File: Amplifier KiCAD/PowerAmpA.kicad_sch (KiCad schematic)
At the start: 39 parts, among them Q1 BC546, Q10 TIP36, Q2 BC546, Q3 BCM846BS-7, Q4 BC546, Q5 BD140, Q6 BC546, Q7 BD140, Q8 TIP35, Q9 BD139

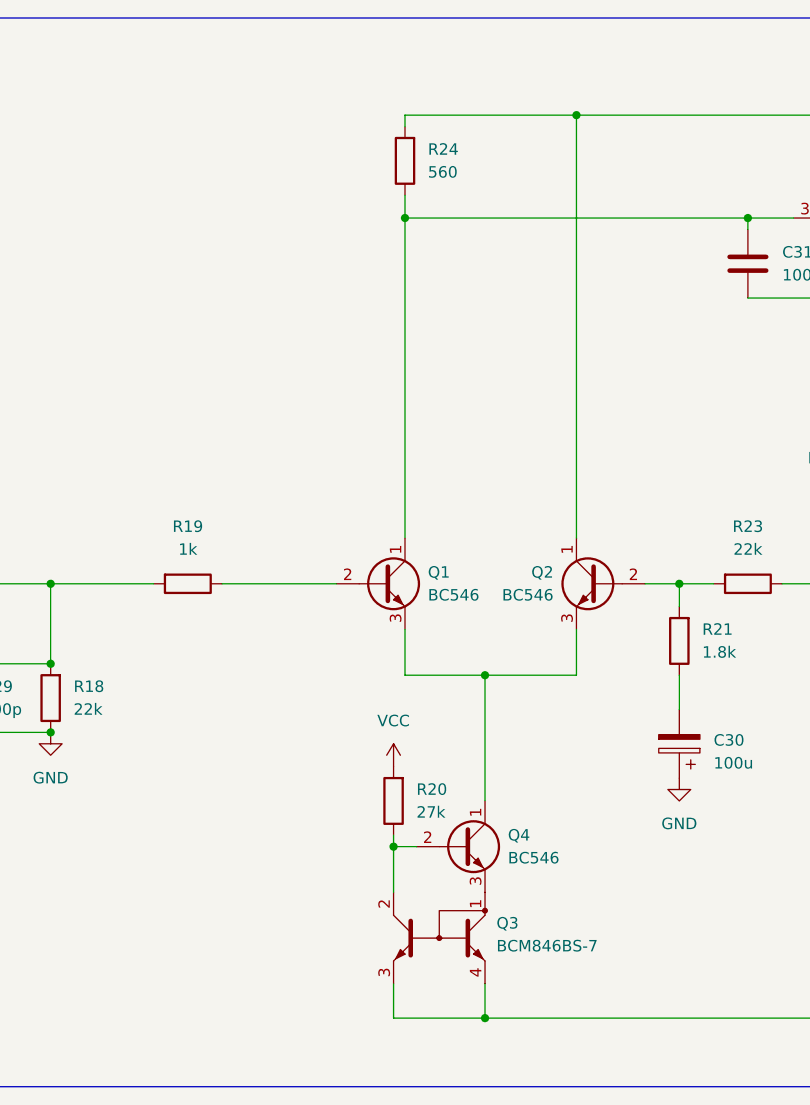
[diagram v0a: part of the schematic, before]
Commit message: Component Placement Finalised, Starting Traces
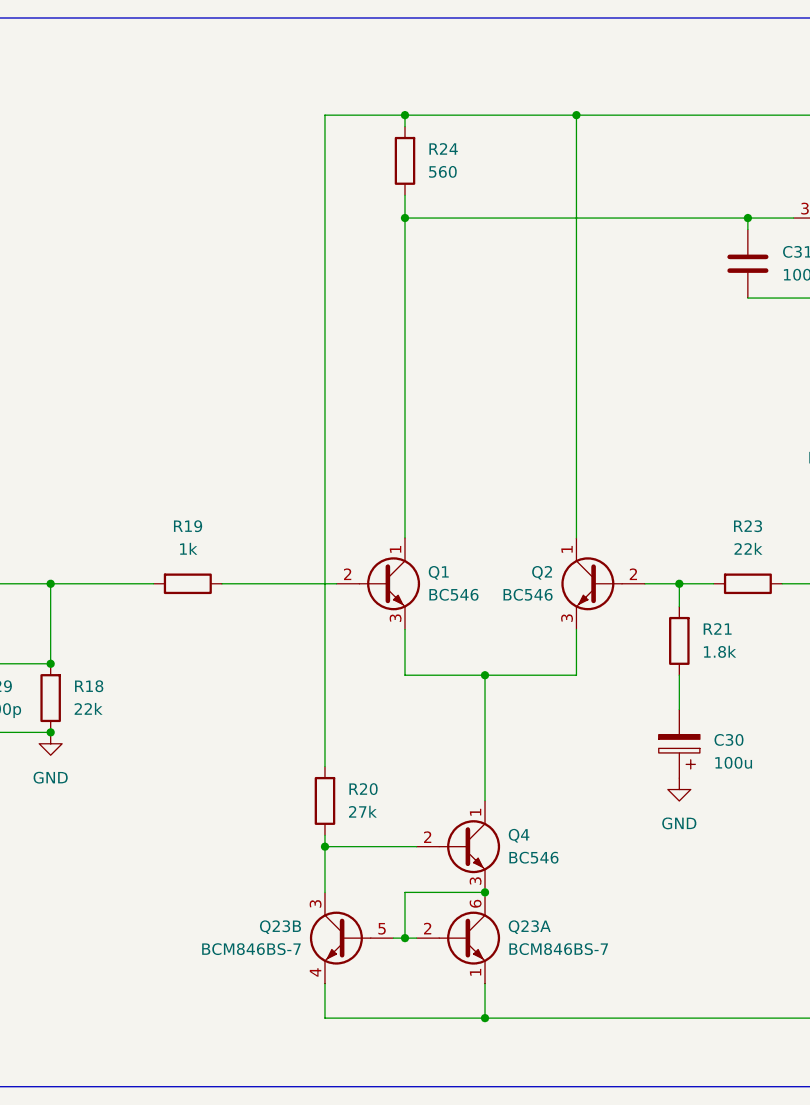
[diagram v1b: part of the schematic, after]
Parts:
- removed Q3: BCM846BS-7, Package_TO_SOT_SMD:SOT-363_SC-70-6, symbol Transistor_BJT:Q_Dual_NPN_C2C1E1E2
- added Q23: BCM846BS-7, Package_TO_SOT_SMD:SOT-363_SC-70-6, symbol Transistor_BJT:Q_Dual_NPN_NPN_C1E1C2E2B2B1
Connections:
- net VCC: no longer R20.2
- net at C35.1, C36.2, F2.1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: now also Q23.1 (E1), Q23.4 (E2)
- net at C37.2, C38.1, F1.1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: now also R20.2
- net at Q4.2 (B), R20.1: now also Q23.3 (C2)
- net at Q4.3 (E): now also Q23.2 (B1), Q23.5 (B2), Q23.6 (C1)
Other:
- moved on the sheet: R20
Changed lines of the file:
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@@
 	)
 	(junction
+		(at 110.49 41.91)
+		(diameter 0)
+		(color 0 0 0 0)
+	)
+	(junction
 		(at 71.12 102.87)
 		(diameter 0)
@@
 	)
 	(junction
-		(at 109.22 123.19)
+		(at 101.6 123.19)
 		(diameter 0)
 		(color 0 0 0 0)
@@
 	)
 	(junction
+		(at 119.38 128.27)
+		(diameter 0)
+		(color 0 0 0 0)
+	)
+	(junction
 		(at 161.29 62.23)
 		(diameter 0)
@@
 	)
 	(junction
-		(at 161.29 87.63)
+		(at 119.38 142.24)
 		(diameter 0)
 		(color 0 0 0 0)
 	)
 	(junction
-		(at 119.38 142.24)
+		(at 110.49 133.35)
+		(diameter 0)
+		(color 0 0 0 0)
+	)
+	(junction
+		(at 161.29 87.63)
 		(diameter 0)
 		(color 0 0 0 0)
@@
 	(wire
 		(pts
-			(xy 109.22 123.19) (xy 109.22 128.27)
+			(xy 101.6 123.19) (xy 101.6 128.27)
 		)
 		(stroke
@@
 	(wire
 		(pts
+			(xy 109.22 133.35) (xy 110.49 133.35)
+		)
+		(stroke
+			(width 0)
+			(type default)
+		)
+	)
+	(wire
+		(pts
 			(xy 218.44 69.85) (xy 218.44 86.36)
 		)
@@
 	(wire
 		(pts
+			(xy 101.6 41.91) (xy 110.49 41.91)
+		)
+		(stroke
+			(width 0)
+			(type default)
+		)
+	)
+	(wire
+		(pts
 			(xy 161.29 106.68) (xy 161.29 107.95)
 		)
@@
 	(wire
 		(pts
+			(xy 110.49 128.27) (xy 119.38 128.27)
+		)
+		(stroke
+			(width 0)
+			(type default)
+		)
+	)
+	(wire
+		(pts
 			(xy 199.39 69.85) (xy 218.44 69.85)
 		)
@@
 	(wire
 		(pts
-			(xy 109.22 142.24) (xy 119.38 142.24)
+			(xy 101.6 142.24) (xy 119.38 142.24)
 		)
 		(stroke
@@
 	(wire
 		(pts
-			(xy 109.22 121.92) (xy 109.22 123.19)
+			(xy 101.6 121.92) (xy 101.6 123.19)
+		)
+		(stroke
+			(width 0)
+			(type default)
+		)
+	)
+	(wire
+		(pts
+			(xy 101.6 138.43) (xy 101.6 142.24)
 		)
 		(stroke
@@
 	(wire
 		(pts
-			(xy 109.22 138.43) (xy 109.22 142.24)
+			(xy 110.49 133.35) (xy 110.49 128.27)
+		)
+		(stroke
+			(width 0)
+			(type default)
+		)
+	)
+	(wire
+		(pts
+			(xy 110.49 133.35) (xy 111.76 133.35)
 		)
 		(stroke
@@
 	(wire
 		(pts
+			(xy 101.6 114.3) (xy 101.6 41.91)
+		)
+		(stroke
+			(width 0)
+			(type default)
+		)
+	)
+	(wire
+		(pts
 			(xy 161.29 142.24) (xy 119.38 142.24)
 		)
@@
 	(wire
 		(pts
-			(xy 109.22 123.19) (xy 111.76 123.19)
+			(xy 101.6 123.19) (xy 111.76 123.19)
 		)
 		(stroke
@@
 	)
 	(symbol
-		(lib_id "power:VCC")
-		(at 109.22 114.3 0)
+		(lib_id "Transistor_BJT:Q_Dual_NPN_NPN_C1E1C2E2B2B1")
+		(at 116.84 133.35 0)
 		(unit 1)
 		(body_style 1)
@@
 		(dnp no)
 		(fields_autoplaced yes)
-		(property "Reference" "#PWR050"
-			(at 109.22 118.11 0)
-			(hide yes)
+		(property "Reference" "Q23"
+			(at 121.92 132.0799 0)
 			(show_name no)
 			(do_not_autoplace no)
@@
 					(size 1.27 1.27)
 				)
+				(justify left)
 			)
 		)
-		(property "Value" "VCC"
-			(at 109.22 109.22 0)
+		(property "Value" "BCM846BS-7"
+			(at 121.92 134.6199 0)
 			(show_name no)
 			(do_not_autoplace no)
@@
 					(size 1.27 1.27)
 				)
+				(justify left)
 			)
 		)
-		(property "Footprint" ""
-			(at 109.22 114.3 0)
+		(property "Footprint" "Package_TO_SOT_SMD:SOT-363_SC-70-6"
+			(at 121.92 130.81 0)
 			(hide yes)
 			(show_name no)
@@
 		)
 		(property "Datasheet" ""
-			(at 109.22 114.3 0)
+			(at 116.84 133.35 0)
 			(hide yes)
 			(show_name no)
@@
 			)
 		)
-		(property "Description" "Power symbol creates a global label with name \"VCC\""
-			(at 109.22 114.3 0)
+		(property "Description" "Dual NPN transistor, 6 pin package"
+			(at 116.84 133.35 0)
 			(hide yes)
 			(show_name no)
@@
 			)
 		)
+		(pin "5"
+		)
+		(pin "3"
+		)
+		(pin "2"
+		)
+		(pin "6"
+		)
+		(pin "4"
+		)
 		(pin "1"
 		)
 		(instances
-			(project "FrontPanelDesign"
-				(path "/90a87c26-e370-4093-aa0b-bbd605aa66f2/1c187844-a6ce-4df2-85bf-61f66b632371"
-					(reference "#PWR050")
-					(unit 1)
-				)
-			)
 			(project "amplifier"
 				(path "/a27a8fa3-29ad-452d-9f63-3f19557e2bab/1c187844-a6ce-4df2-85bf-61f66b632371"
-					(reference "#PWR050")
+					(reference "Q23")
 					(unit 1)
 				)
@@
 	)
 	(symbol
-		(lib_id "Transistor_BJT:Q_Dual_NPN_C2C1E1E2")
-		(at 114.3 133.35 0)
-		(mirror y)
-		(unit 1)
-		(body_style 1)
-		(exclude_from_sim no)
-		(in_bom yes)
-		(on_board yes)
-		(in_pos_files yes)
-		(dnp no)
-		(fields_autoplaced yes)
-		(property "Reference" "Q3"
-			(at 120.65 131.6989 0)
-			(show_name no)
-			(do_not_autoplace no)
-			(effects
-				(font
-					(size 1.27 1.27)
-				)
-				(justify right)
-			)
-		)
-		(property "Value" "BCM846BS-7"
-			(at 120.65 134.2389 0)
-			(show_name no)
-			(do_not_autoplace no)
-			(effects
-				(font
-					(size 1.27 1.27)
-				)
-				(justify right)
-			)
-		)
-		(property "Footprint" "Package_TO_SOT_SMD:SOT-363_SC-70-6"
-			(at 114.3 133.35 0)
-			(hide yes)
-			(show_name no)
-			(do_not_autoplace no)
-			(effects
-				(font
-					(size 1.27 1.27)
-					(italic yes)
-				)
-			)
-		)
-		(property "Datasheet" ""
-			(at 116.84 133.35 0)
-			(hide yes)
-			(show_name no)
-			(do_not_autoplace no)
-			(effects
-				(font
-					(size 1.27 1.27)
-				)
-				(justify left)
-			)
-		)
-		(property "Description" "Double NPN transistors, current mirror configuration"
-			(at 114.3 133.35 0)
-			(hide yes)
-			(show_name no)
-			(do_not_autoplace no)
-			(effects
-				(font
-					(size 1.27 1.27)
-				)
-			)
-		)
-		(pin "1"
-		)
-		(pin "3"
-		)
-		(pin "4"
-		)
-		(pin "2"
-		)
-		(instances
-			(project "FrontPanelDesign"
-				(path "/90a87c26-e370-4093-aa0b-bbd605aa66f2/1c187844-a6ce-4df2-85bf-61f66b632371"
-					(reference "Q3")
-					(unit 1)
-				)
-			)
-			(project "amplifier"
-				(path "/a27a8fa3-29ad-452d-9f63-3f19557e2bab/1c187844-a6ce-4df2-85bf-61f66b632371"
-					(reference "Q3")
-					(unit 1)
-				)
-			)
-		)
-	)
-	(symbol
 		(lib_id "Transistor_BJT:BD140")
 		(at 199.39 106.68 0)
@@
 	)
 	(symbol
+		(lib_name "Q_Dual_NPN_NPN_C1E1C2E2B2B1_1")
+		(lib_id "Transistor_BJT:Q_Dual_NPN_NPN_C1E1C2E2B2B1")
+		(at 104.14 133.35 0)
+		(mirror y)
+		(unit 2)
+		(body_style 1)
+		(exclude_from_sim no)
+		(in_bom yes)
+		(on_board yes)
+		(in_pos_files yes)
+		(dnp no)
+		(fields_autoplaced yes)
+		(property "Reference" "Q23"
+			(at 99.06 132.0799 0)
+			(show_name no)
+			(do_not_autoplace no)
+			(effects
+				(font
+					(size 1.27 1.27)
+				)
+				(justify left)
+			)
+		)
+		(property "Value" "BCM846BS-7"
+			(at 99.06 134.6199 0)
+			(show_name no)
+			(do_not_autoplace no)
+			(effects
+				(font
+					(size 1.27 1.27)
+				)
+				(justify left)
+			)
+		)
+		(property "Footprint" "Package_TO_SOT_SMD:SOT-363_SC-70-6"
+			(at 99.06 130.81 0)
+			(hide yes)
+			(show_name no)
+			(do_not_autoplace no)
+			(effects
+				(font
+					(size 1.27 1.27)
+				)
+			)
+		)
+		(property "Datasheet" ""
+			(at 104.14 133.35 0)
+			(hide yes)
+			(show_name no)
+			(do_not_autoplace no)
+			(effects
+				(font
+					(size 1.27 1.27)
+				)
+			)
+		)
+		(property "Description" "Dual NPN transistor, 6 pin package"
+			(at 104.14 133.35 0)
+			(hide yes)
+			(show_name no)
+			(do_not_autoplace no)
+			(effects
+				(font
+					(size 1.27 1.27)
+				)
+			)
+		)
+		(pin "5"
+		)
+		(pin "3"
+		)
+		(pin "2"
+		)
+		(pin "1"
+		)
+		(pin "4"
+		)
+		(pin "6"
+		)
+		(instances
+			(project "amplifier"
+				(path "/a27a8fa3-29ad-452d-9f63-3f19557e2bab/1c187844-a6ce-4df2-85bf-61f66b632371"
+					(reference "Q23")
+					(unit 2)
+				)
+			)
+		)
+	)
+	(symbol
 		(lib_id "Device:R")
-		(at 109.22 118.11 180)
+		(at 101.6 118.11 180)
 		(unit 1)
 		(body_style 1)
@@
 		(fields_autoplaced yes)
 		(property "Reference" "R20"
-			(at 111.76 116.8399 0)
+			(at 104.14 116.8399 0)
 			(show_name no)
 			(do_not_autoplace no)
@@
 		)
 		(property "Value" "27k"
-			(at 111.76 119.3799 0)
+			(at 104.14 119.3799 0)
 			(show_name no)
 			(do_not_autoplace no)
@@
 		)
 		(property "Footprint" "Resistor_THT:R_Axial_DIN0207_L6.3mm_D2.5mm_P10.16mm_Horizontal"
-			(at 110.998 118.11 90)
+			(at 103.378 118.11 90)
 			(hide yes)
 			(show_name no)
@@
 		)
 		(property "Datasheet" ""
-			(at 109.22 118.11 0)
+			(at 101.6 118.11 0)
 			(hide yes)
 			(show_name no)
@@
 		)
 		(property "Description" "Resistor"
-			(at 109.22 118.11 0)
+			(at 101.6 118.11 0)
 			(hide yes)
 			(show_name no)
